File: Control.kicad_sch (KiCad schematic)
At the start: 10 parts, among them J401 Conn_02x05_Odd_Even, M401 Fan_4pin, Q401 BSS138

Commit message: changed pass element drive
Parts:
- added C404: 100n, Capacitor_SMD:C_0603_1608Metric, symbol Device:C
- added R403, R404: 2k, Resistor_SMD:R_0603_1608Metric, symbol Device:R
- added U401: TMP1075D, Package_SO:SO-8_3.9x4.9mm_P1.27mm, symbol Sensor_Temperature:TMP1075D
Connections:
- net CH1_I2C_SCL is gone; now on net SCL: A401.7 (GPIO7)
- net CH1_I2C_SDA is gone; now on net SDA: A401.6 (GPIO6)
- net +3.3V: now also C404.1, R403.2, R404.2, U401.5 (A2), U401.6 (A1), U401.7 (A0), U401.8 (V+)
- net Buzzer: now also A401.27 (GPIO27_ADC1)
- net CS: now also A401.13 (GPIO13); no longer A401.5 (GPIO5)
- net DC: now also A401.12 (GPIO12); no longer A401.4 (GPIO4)
- net FanPWM: now also A401.26 (GPIO26_ADC0)
- net GNDD: now also C404.2, U401.4 (GND)
- net RESET: now also A401.9 (GPIO9); no longer A401.1 (GPIO1)
- net SCK: now also A401.10 (GPIO10); no longer A401.2 (GPIO2)
- net SCL: now also R404.1, U401.2 (SCL)
- net SDA: now also R403.1, U401.1 (SDA)
- net SDI(MOSI): now also A401.11 (GPIO11); no longer A401.3 (GPIO3)
- net ~{INT}: now also A401.8 (GPIO8)
- net Tx_Ch1: now reaches A401.0 (GPIO0)
- net CH2_I2C_SCL: no longer names the net of A401.21 (GPIO21)
- net CH2_I2C_SDA: no longer names the net of A401.20 (GPIO20)
- new net Rx_Ch1: A401.1 (GPIO1)
- new net Rx_Ch2: A401.5 (GPIO5)
- new net Tx_Ch2: A401.4 (GPIO4)

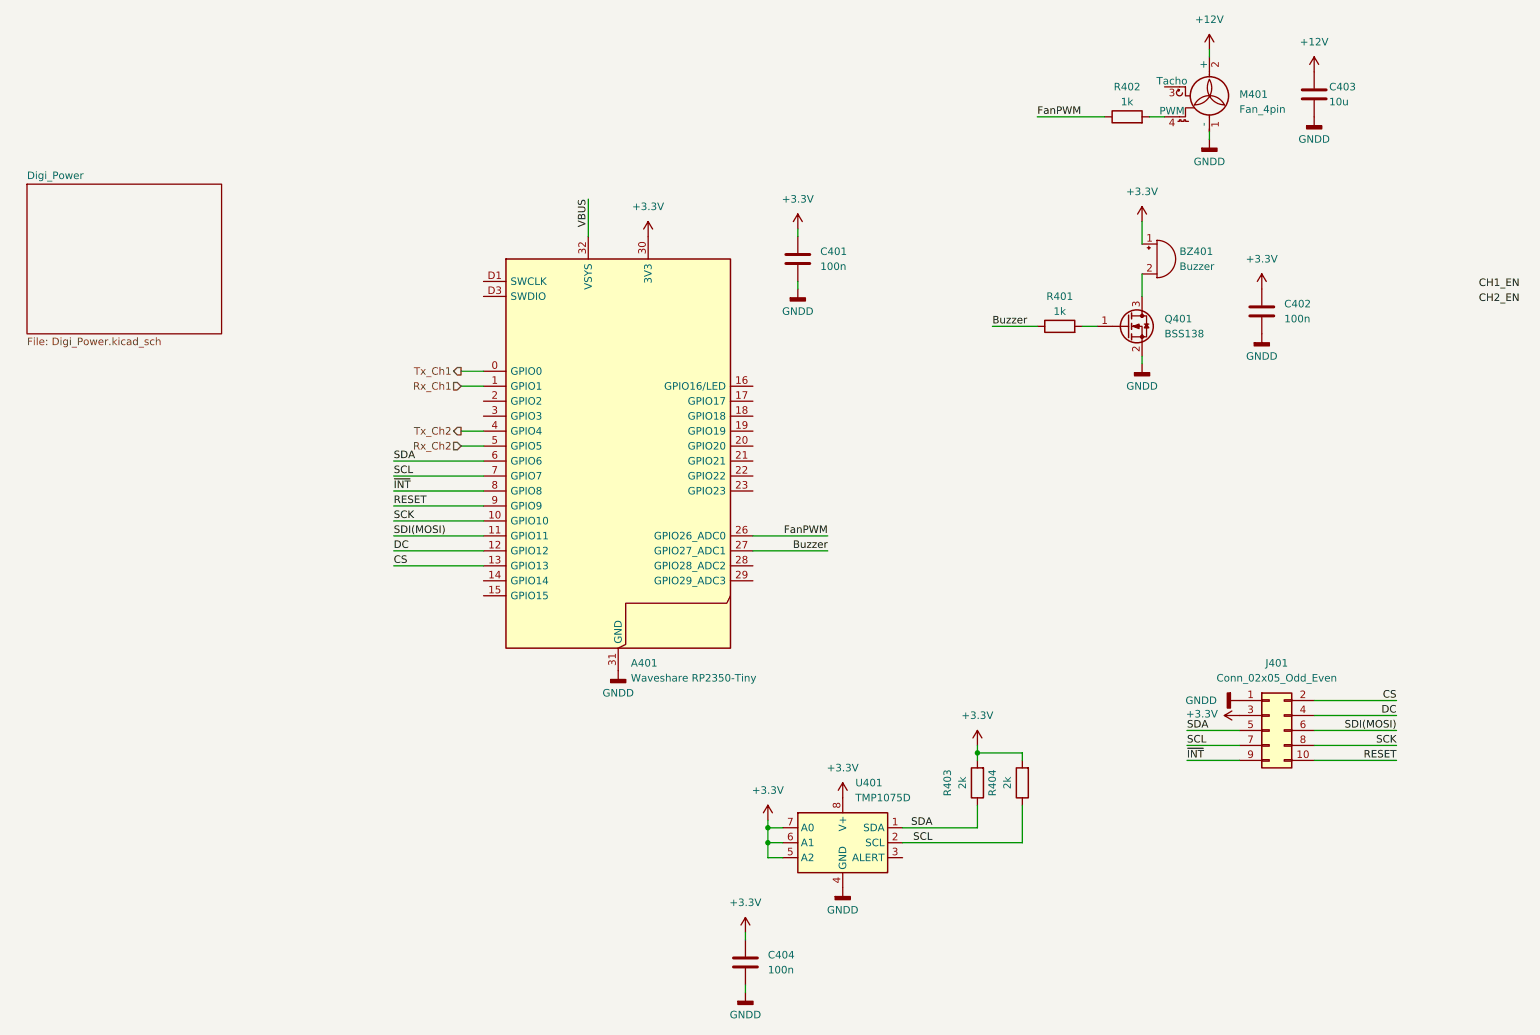
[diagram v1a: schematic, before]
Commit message: added Ch2 and removed global power flags
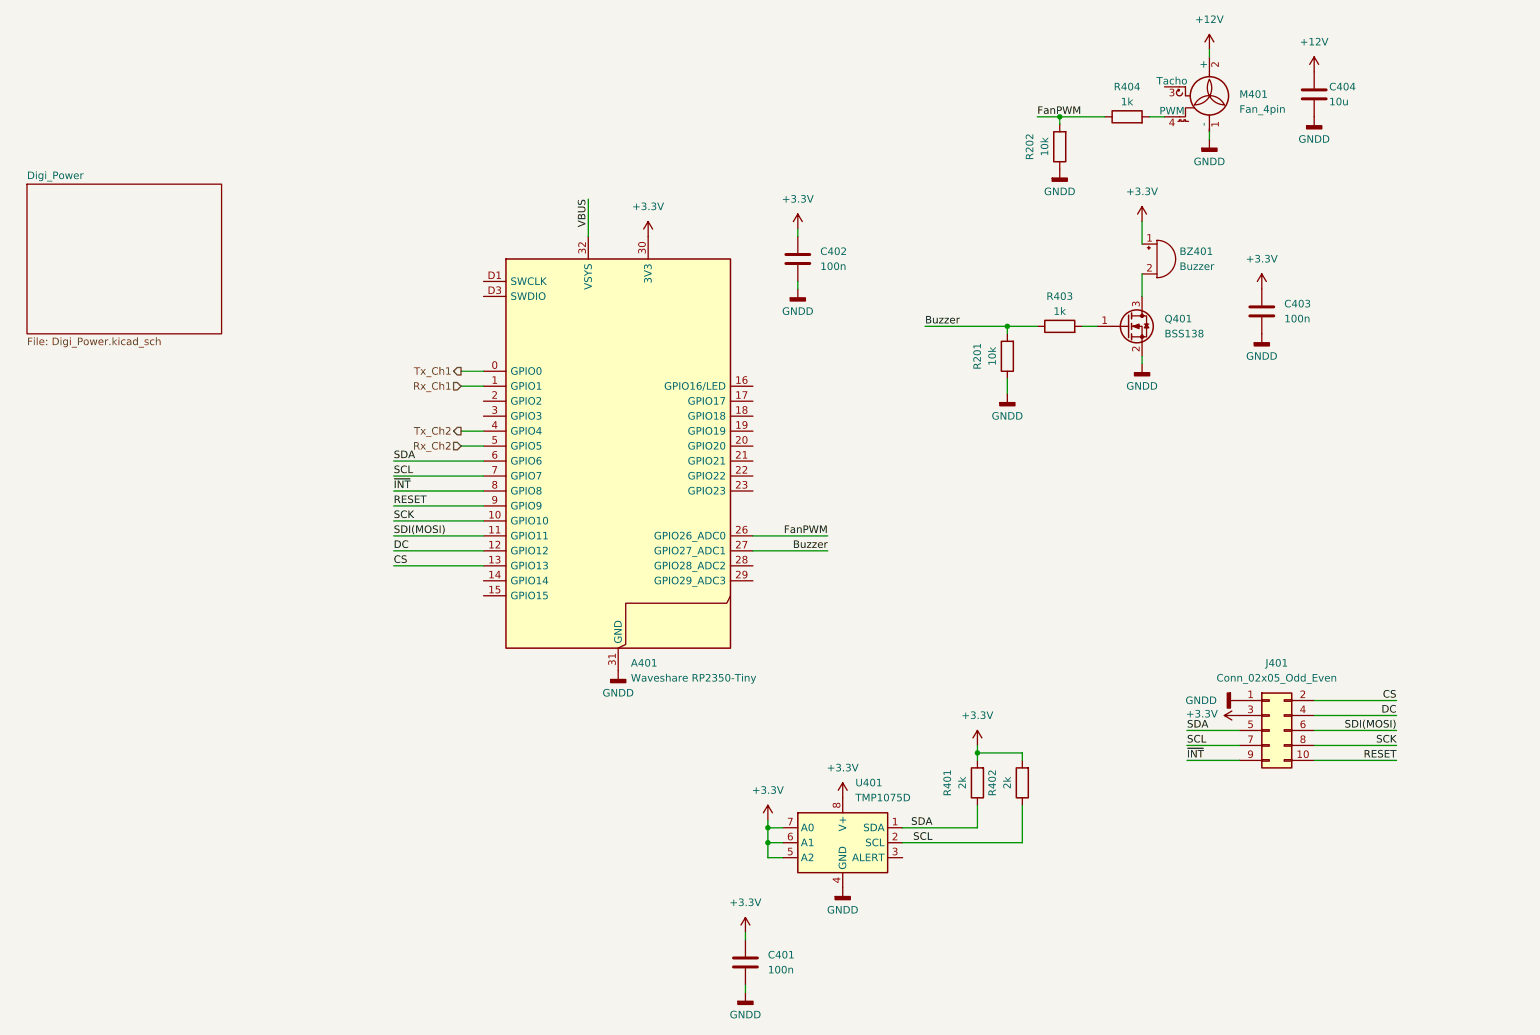
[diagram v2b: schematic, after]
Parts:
- added R201, R202: 10k, Resistor_SMD:R_0603_1608Metric, symbol Device:R
- renumbered C404 to C401, C401 to C402, C402 to C403, C403 to C404, R403 to R401, R404 to R402, R401 to R403, R402 to R404
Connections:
- net Buzzer: now also R201.2
- net FanPWM: now also R202.2
- net GNDD: now also R201.1, R202.1

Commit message: added loop calc
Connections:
- net GNDD: now also J401.5 (Pin_5); no longer J401.1 (Pin_1)
- net SDA: now also J401.1 (Pin_1); no longer J401.5 (Pin_5)
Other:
- moved on the sheet: C403
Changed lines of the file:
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@@
 	(wire
 		(pts
-			(xy 217.17 137.16) (xy 226.06 137.16)
+			(xy 217.17 132.08) (xy 226.06 132.08)
 		)
 		(stroke
@@
 	)
 	(label "SDA"
-		(at 217.17 137.16 0)
+		(at 217.17 132.08 0)
 		(effects
 			(font
@@
 	(symbol
 		(lib_id "Device:C")
-		(at 229.87 66.04 0)
+		(at 232.41 83.82 0)
 		(unit 1)
 		(body_style 1)
@@
 		(fields_autoplaced yes)
 		(property "Reference" "C403"
-			(at 233.68 64.7699 0)
+			(at 236.22 82.5499 0)
 			(show_name no)
 			(do_not_autoplace no)
@@
 		)
 		(property "Value" "100n"
-			(at 233.68 67.3099 0)
+			(at 236.22 85.0899 0)
 			(show_name no)
 			(do_not_autoplace no)
@@
 		)
 		(property "Footprint" "Capacitor_SMD:C_0603_1608Metric"
-			(at 230.8352 69.85 0)
-			(hide yes)
-			(show_name no)
-			(do_not_autoplace no)
-			(effects
-				(font
-					(size 1.27 1.27)
-				)
-			)
-		)
-		(property "Datasheet" ""
-			(at 229.87 66.04 0)
+			(at 233.3752 87.63 0)
+			(hide yes)
+			(show_name no)
+			(do_not_autoplace no)
+			(effects
+				(font
+					(size 1.27 1.27)
+				)
+			)
+		)
+		(property "Datasheet" ""
+			(at 232.41 83.82 0)
 			(hide yes)
 			(show_name no)
@@
 		)
 		(property "Description" "Unpolarized capacitor"
-			(at 229.87 66.04 0)
+			(at 232.41 83.82 0)
 			(hide yes)
 			(show_name no)
@@
 	(symbol
 		(lib_id "power:GNDD")
-		(at 226.06 132.08 270)
+		(at 226.06 137.16 270)
 		(unit 1)
 		(body_style 1)
@@
 		(fields_autoplaced yes)
 		(property "Reference" "#PWR0415"
-			(at 219.71 132.08 0)
+			(at 219.71 137.16 0)
 			(hide yes)
 			(show_name no)
@@
 		)
 		(property "Value" "GNDD"
-			(at 222.25 132.0799 90)
+			(at 222.25 137.1599 90)
 			(show_name no)
 			(do_not_autoplace no)
@@
 		)
 		(property "Footprint" ""
-			(at 226.06 132.08 0)
-			(hide yes)
-			(show_name no)
-			(do_not_autoplace no)
-			(effects
-				(font
-					(size 1.27 1.27)
-				)
-			)
-		)
-		(property "Datasheet" ""
-			(at 226.06 132.08 0)
+			(at 226.06 137.16 0)
+			(hide yes)
+			(show_name no)
+			(do_not_autoplace no)
+			(effects
+				(font
+					(size 1.27 1.27)
+				)
+			)
+		)
+		(property "Datasheet" ""
+			(at 226.06 137.16 0)
 			(hide yes)
 			(show_name no)
@@
 		)
 		(property "Description" "Power symbol creates a global label with name \"GNDD\" , digital ground"
-			(at 226.06 132.08 0)
+			(at 226.06 137.16 0)
 			(hide yes)
 			(show_name no)
@@
 	(symbol
 		(lib_id "power:GNDD")
-		(at 229.87 69.85 0)
+		(at 232.41 87.63 0)
 		(unit 1)
 		(body_style 1)
@@
 		(fields_autoplaced yes)
 		(property "Reference" "#PWR0418"
-			(at 229.87 76.2 0)
+			(at 232.41 93.98 0)
 			(hide yes)
 			(show_name no)
@@
 		)
 		(property "Value" "GNDD"
-			(at 229.87 73.66 0)
+			(at 232.41 91.44 0)
 			(show_name no)
 			(do_not_autoplace no)
@@
 		)
 		(property "Footprint" ""
-			(at 229.87 69.85 0)
-			(hide yes)
-			(show_name no)
-			(do_not_autoplace no)
-			(effects
-				(font
-					(size 1.27 1.27)
-				)
-			)
-		)
-		(property "Datasheet" ""
-			(at 229.87 69.85 0)
+			(at 232.41 87.63 0)
+			(hide yes)
+			(show_name no)
+			(do_not_autoplace no)
+			(effects
+				(font
+					(size 1.27 1.27)
+				)
+			)
+		)
+		(property "Datasheet" ""
+			(at 232.41 87.63 0)
 			(hide yes)
 			(show_name no)
@@
 		)
 		(property "Description" "Power symbol creates a global label with name \"GNDD\" , digital ground"
-			(at 229.87 69.85 0)
+			(at 232.41 87.63 0)
 			(hide yes)
 			(show_name no)
@@
 	(symbol
 		(lib_id "power:+3.3V")
-		(at 229.87 62.23 0)
+		(at 232.41 80.01 0)
 		(unit 1)
 		(body_style 1)
@@
 		(fields_autoplaced yes)
 		(property "Reference" "#PWR0417"
-			(at 229.87 66.04 0)
+			(at 232.41 83.82 0)
 			(hide yes)
 			(show_name no)
@@
 		)
 		(property "Value" "+3.3V"
-			(at 229.87 57.15 0)
+			(at 232.41 74.93 0)
 			(show_name no)
 			(do_not_autoplace no)
@@
 		)
 		(property "Footprint" ""
-			(at 229.87 62.23 0)
-			(hide yes)
-			(show_name no)
-			(do_not_autoplace no)
-			(effects
-				(font
-					(size 1.27 1.27)
-				)
-			)
-		)
-		(property "Datasheet" ""
-			(at 229.87 62.23 0)
+			(at 232.41 80.01 0)
+			(hide yes)
+			(show_name no)
+			(do_not_autoplace no)
+			(effects
+				(font
+					(size 1.27 1.27)
+				)
+			)
+		)
+		(property "Datasheet" ""
+			(at 232.41 80.01 0)
 			(hide yes)
 			(show_name no)
@@
 		)
 		(property "Description" "Power symbol creates a global label with name \"+3.3V\""
-			(at 229.87 62.23 0)
-			(hide yes)
-			(show_name no)
+			(at 232.41 80.01 0)
+			(hide yes)
+			(show_name no)

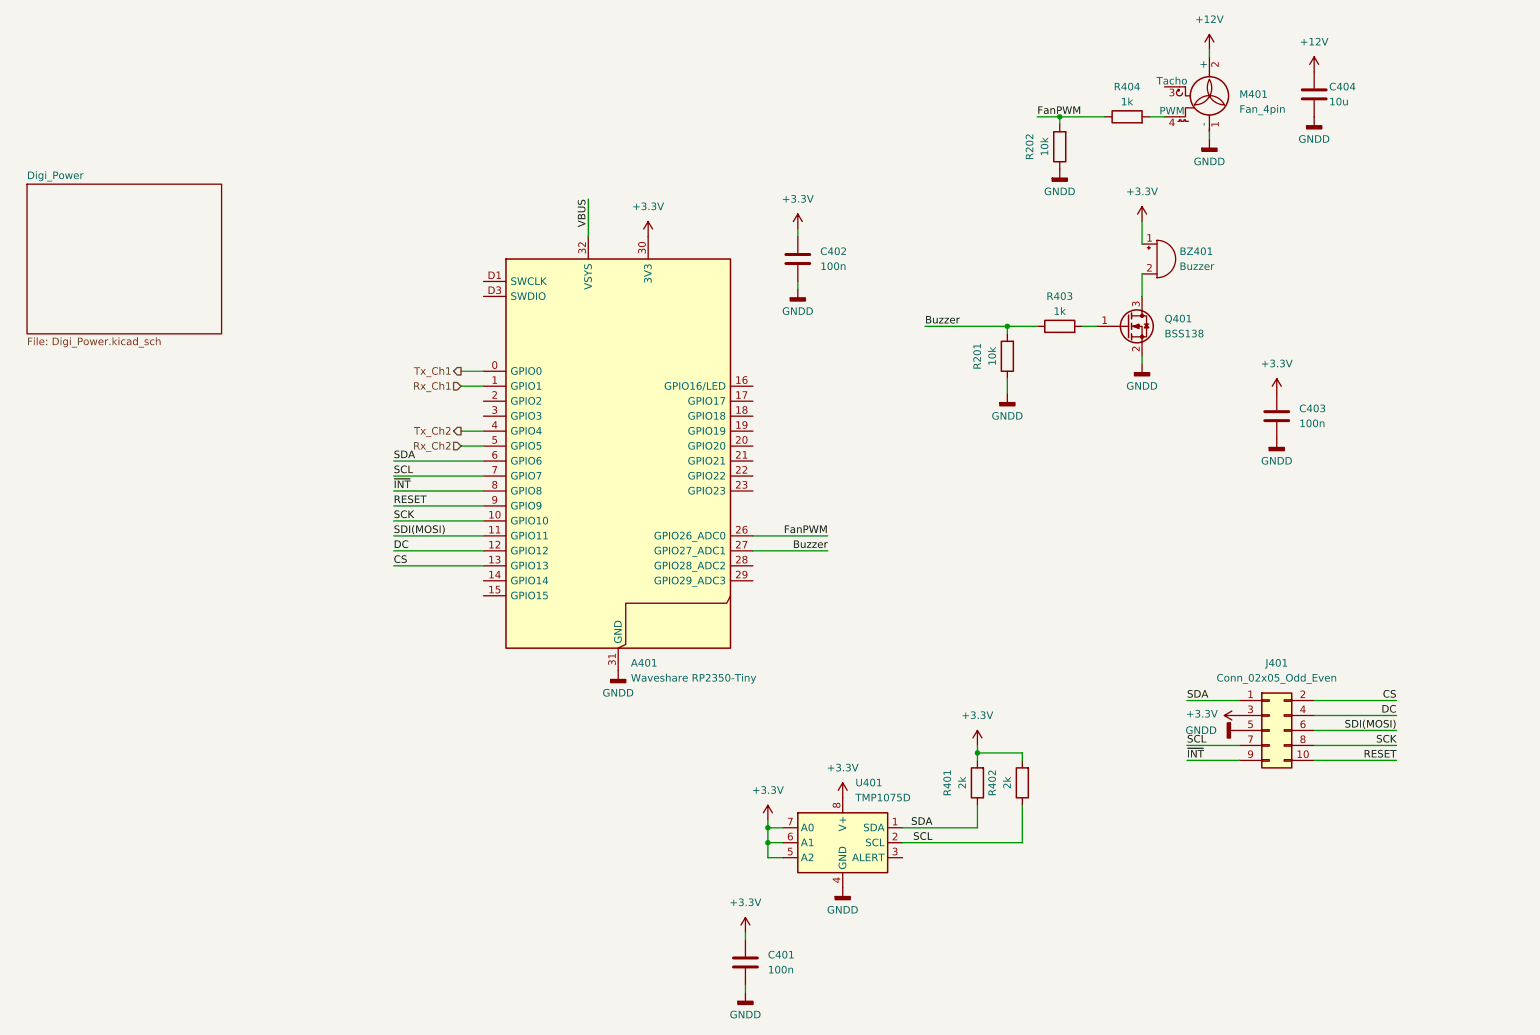
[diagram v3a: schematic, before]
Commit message: add adc and dac estimate
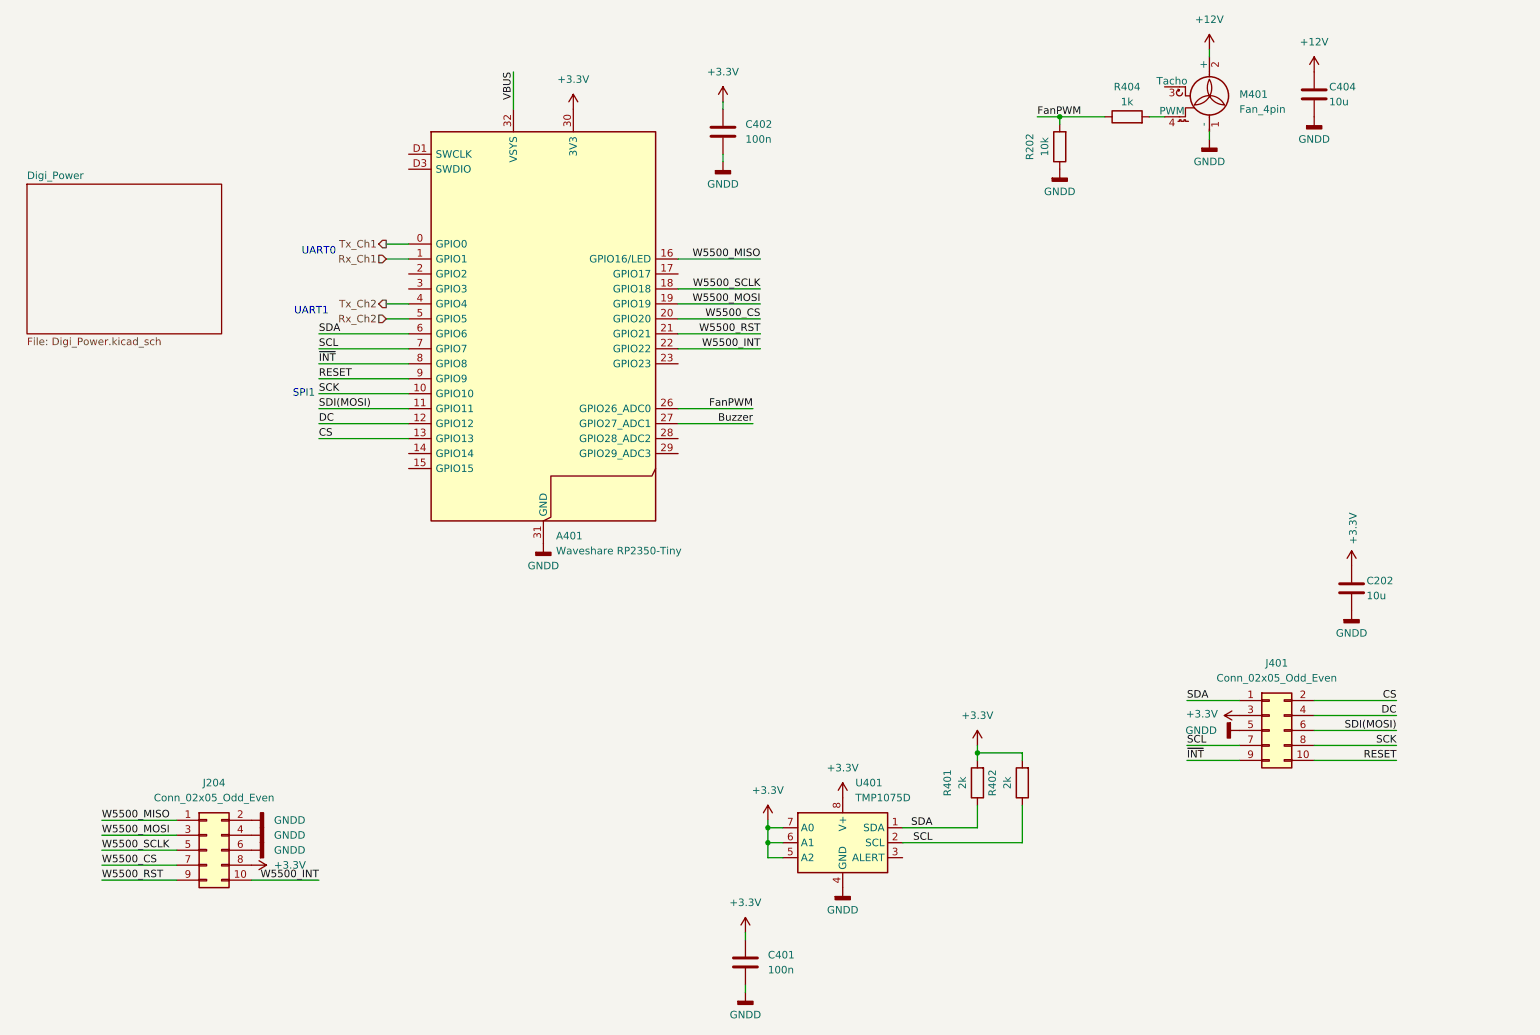
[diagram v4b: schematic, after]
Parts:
- removed BZ401: Buzzer, Buzzer_Beeper:Buzzer_12x9.5RM7.6, symbol Device:Buzzer
- removed C403: 100n, Capacitor_SMD:C_0603_1608Metric, symbol Device:C
- removed Q401: BSS138, Package_TO_SOT_SMD:SOT-23-3, symbol Transistor_FET:BSS138
- removed R201: 10k, Resistor_SMD:R_0603_1608Metric, symbol Device:R
- removed R403: 1k, Resistor_SMD:R_0603_1608Metric, symbol Device:R
- added C202: 10u, Capacitor_SMD:C_0805_2012Metric, symbol Device:C
- added J204: Conn_02x05_Odd_Even, Connector_IDC:IDC-Header_2x05_P2.54mm_Vertical, symbol Connector_Generic:Conn_02x05_Odd_Even
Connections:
- net +3.3V: now also C202.1, J204.8 (Pin_8)
- net GNDD: now also C202.2, J204.2 (Pin_2), J204.4 (Pin_4), J204.6 (Pin_6)
- net W5500_MISO: now reaches A401.16 (GPIO16/LED)
- net W5500_MISO: now also J204.1 (Pin_1)
- net W5500_SCLK: now reaches A401.18 (GPIO18)
- net W5500_SCLK: now also J204.5 (Pin_5)
- net W5500_MOSI: now reaches A401.19 (GPIO19)
- net W5500_MOSI: now also J204.3 (Pin_3)
- net W5500_CS: now reaches A401.20 (GPIO20)
- net W5500_CS: now also J204.7 (Pin_7)
- net W5500_RST: now reaches A401.21 (GPIO21)
- net W5500_RST: now also J204.9 (Pin_9)
- net W5500_INT: now reaches A401.22 (GPIO22)
- net W5500_INT: now also J204.10 (Pin_10)
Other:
- note added: "SPI1"
- note added: "UART0"
- note added: "UART1"
- moved on the sheet: A401, C402

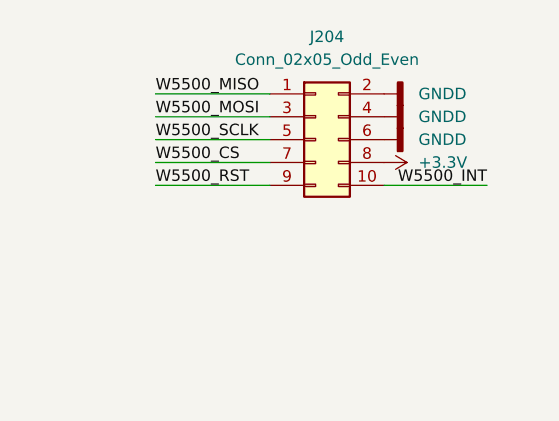
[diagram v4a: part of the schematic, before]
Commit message: add diodes for clamping
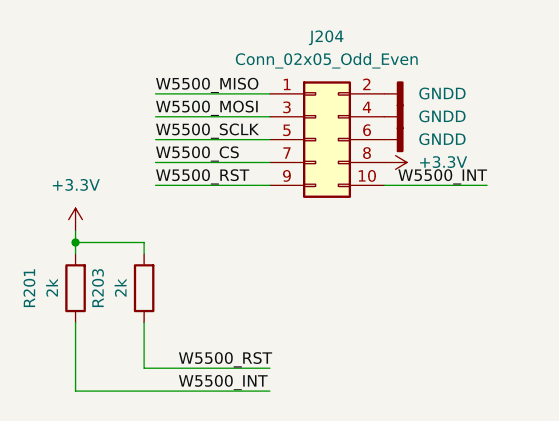
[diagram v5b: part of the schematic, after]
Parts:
- added R201, R203: 2k, Resistor_SMD:R_0603_1608Metric, symbol Device:R
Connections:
- net +3.3V: now also R201.2, R203.2
- net W5500_INT: now also R201.1
- net W5500_RST: now also R203.1
